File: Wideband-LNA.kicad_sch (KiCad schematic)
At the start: 23 parts, among them J1 Conn_Coaxial, J2 Conn_Coaxial, J3 USB_C_Receptacle_USB2.0_16P, U1 TQP3M9037, U2 AP2127K-ADJ

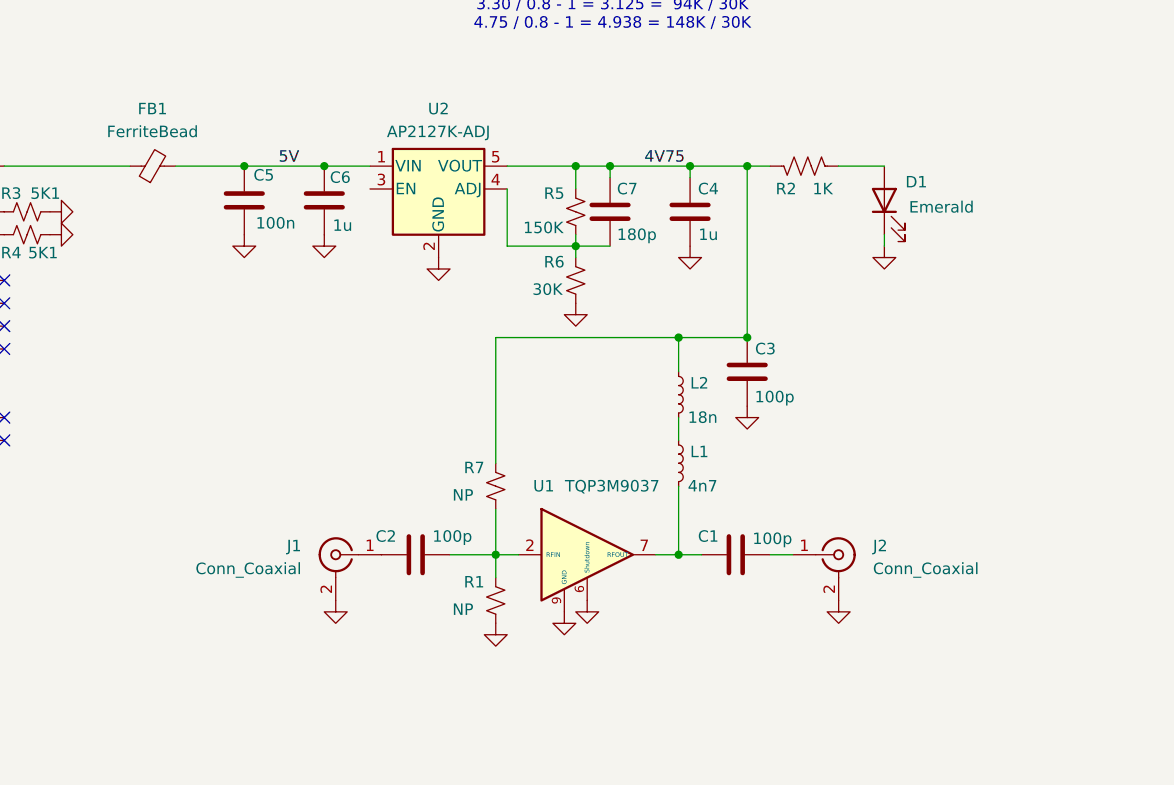
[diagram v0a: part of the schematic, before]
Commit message: rename datasheets, tweak layout
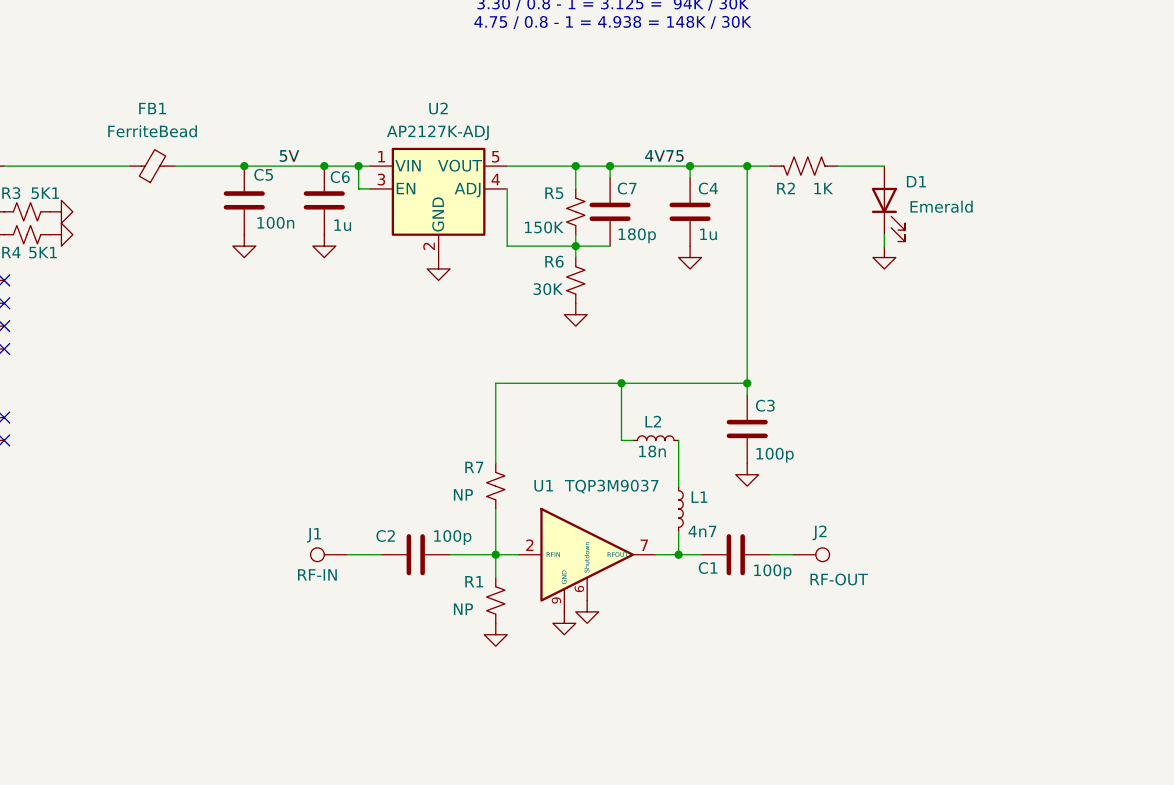
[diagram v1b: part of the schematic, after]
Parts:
- removed J1, J2: Conn_Coaxial, wa1hco:SMA_Amphenol_132289_EdgeMount, symbol Connector:Conn_Coaxial
- added J1: RF-IN, TestPoint:TestPoint_Pad_1.0x1.0mm, symbol Connector:TestPoint
- added J2: RF-OUT, TestPoint:TestPoint_Pad_1.0x1.0mm, symbol Connector:TestPoint
- J3: footprint Connector_USB:USB_C_Receptacle_HCTL_HC-TYPE-C-16P-01A -> wa1hco:USB_C_Receptacle_G-Switch_GT-USB-7010ASV
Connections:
- net 5V: now also U2.3 (EN)
- net at C1.2: now also J2.1
- net at C2.1: now also J1.1
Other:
- moved on the sheet: C3, L1, L2

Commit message: changed to 50 to 2000 MHz, qorvo 9036, 68 nH choke
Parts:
- removed R1, R7: NP, Resistor_SMD:R_0402_1005Metric, symbol Device:R_Small_US
- L2: value 18n -> 68n

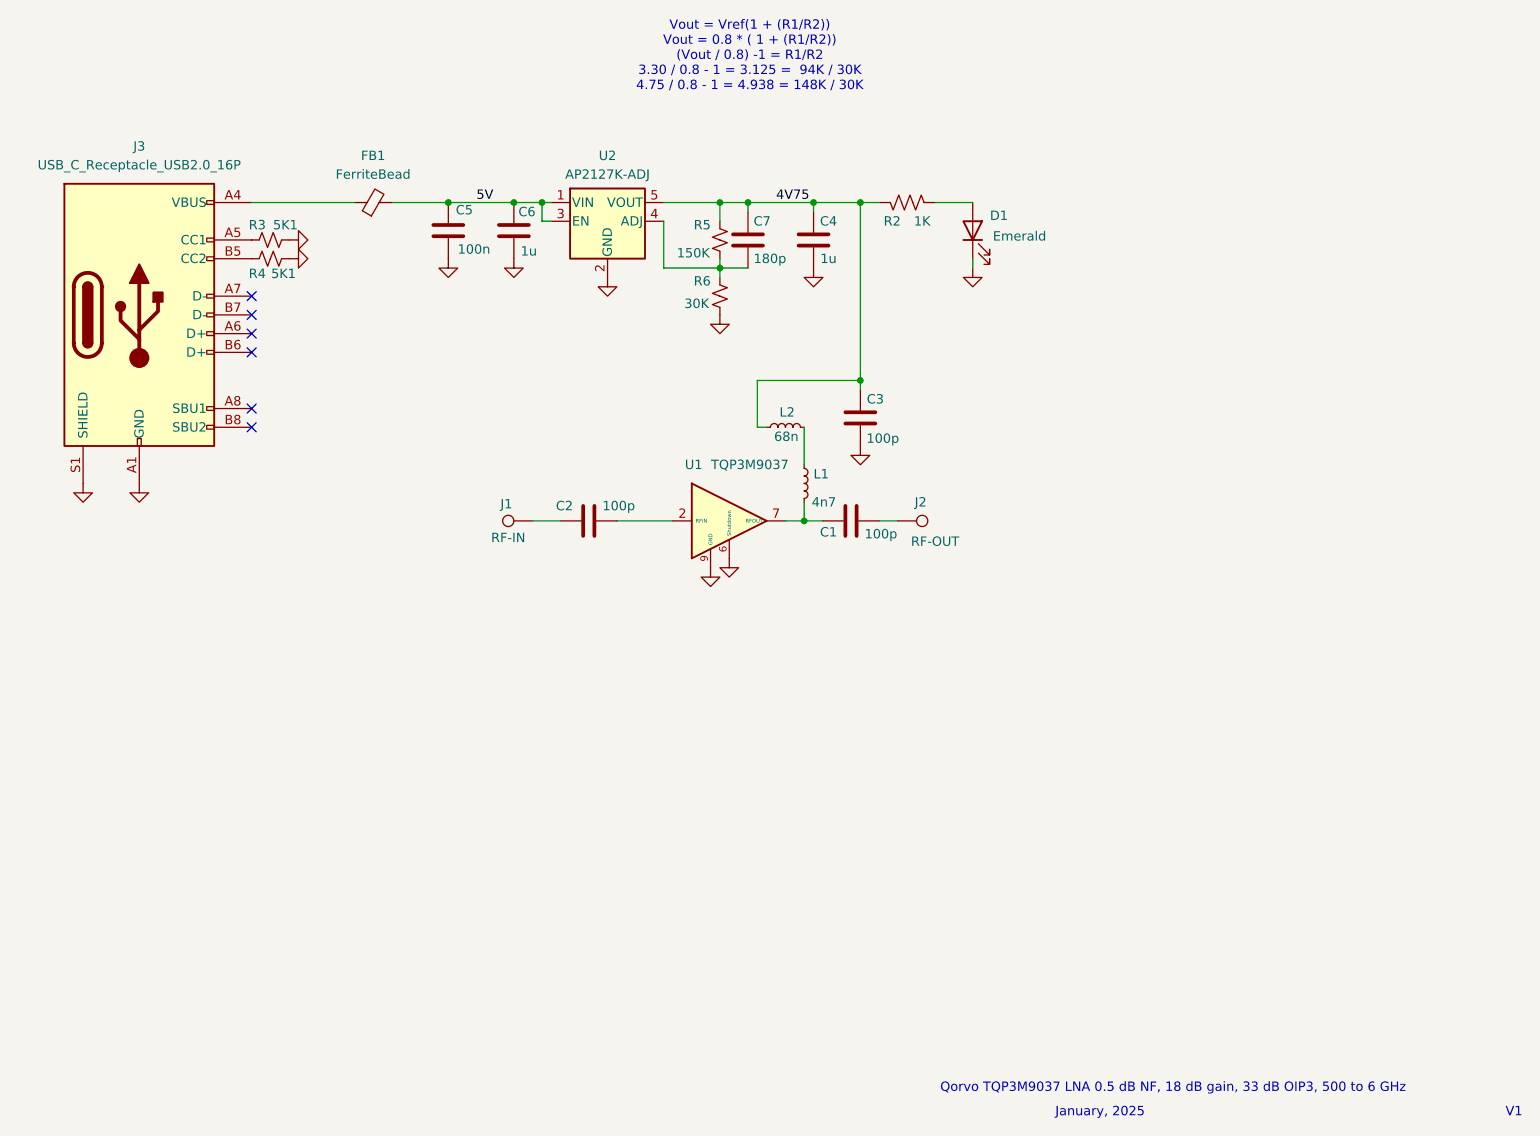
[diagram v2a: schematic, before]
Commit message: M2 screw hole from via to mounting hole Increased radius of corners Reduced side to 18.8 mm to allow clearance in enclosure Increase size of notch for SMA pin Added into to back silkscreen
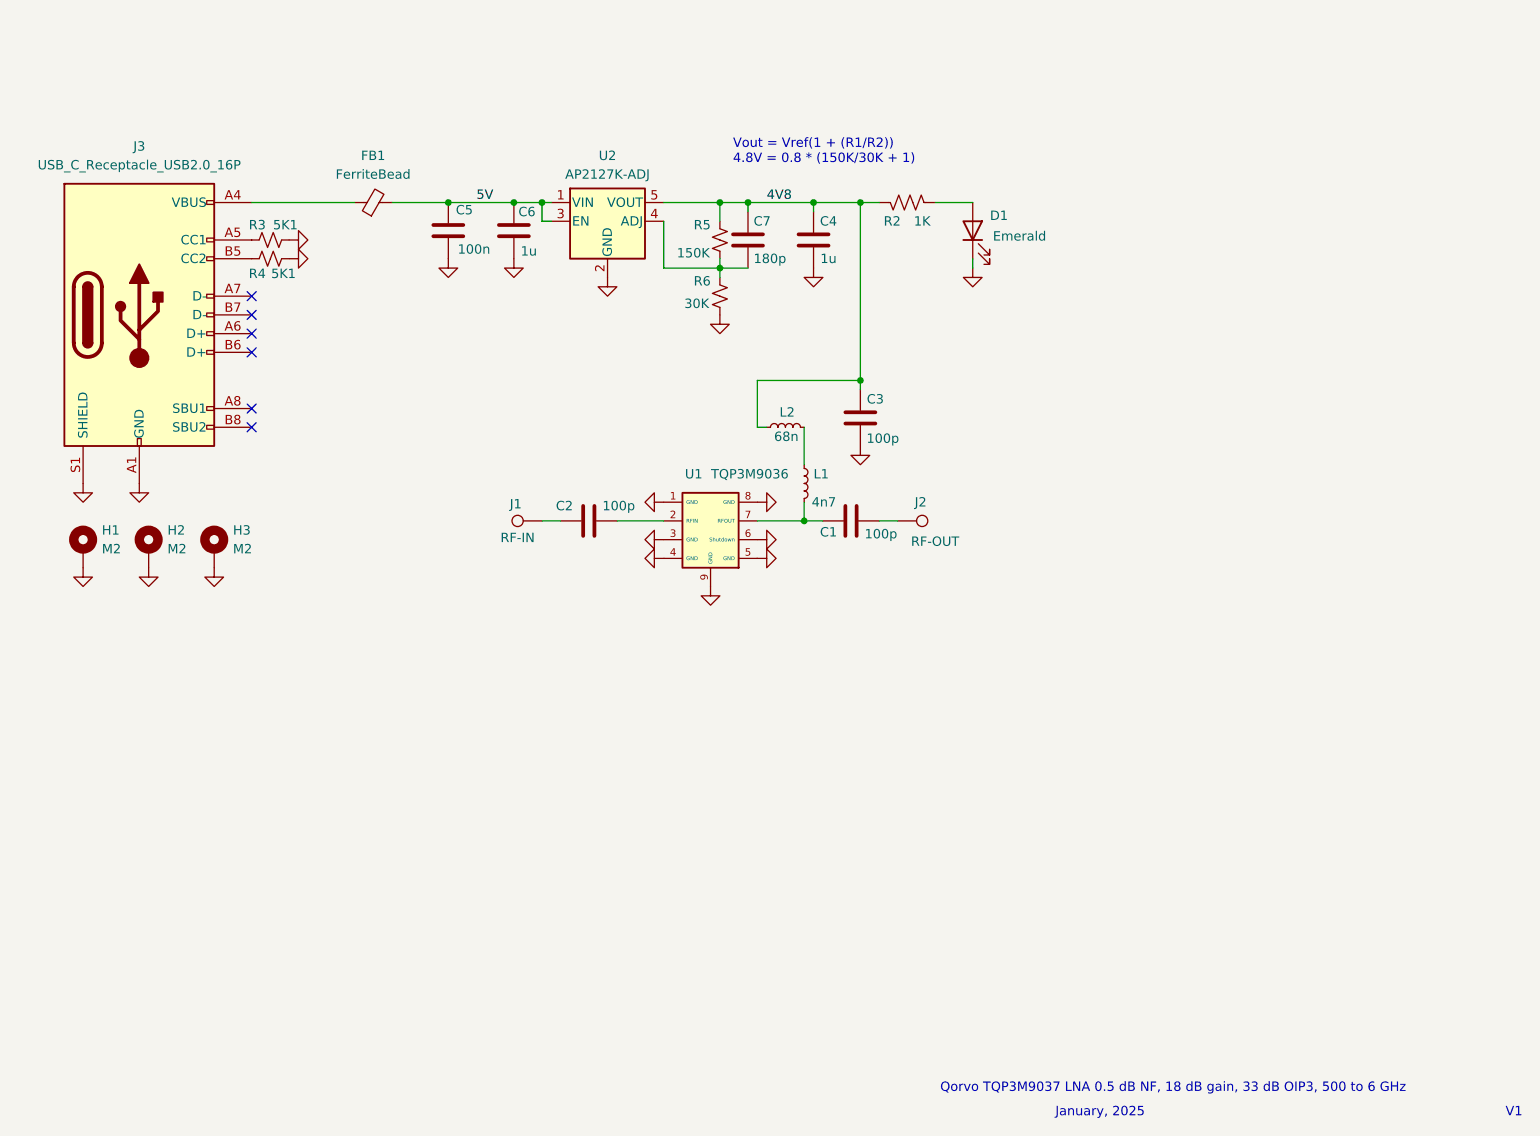
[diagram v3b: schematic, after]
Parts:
- added H1, H2, H3: M2, MountingHole:MountingHole_2.2mm_M2_DIN965_Pad, symbol Mechanical:MountingHole_Pad
- L2: LCSC C405066 -> C405073
- U1: value TQP3M9037 -> TQP3M9036; symbol wa1hco:TQP3M9037 -> wa1hco:TQP3M9036; LCSC C415712 -> C920261
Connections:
- net GND: now also U1.1 (GND), U1.3 (GND), U1.4 (GND), U1.5 (GND), U1.8 (GND), H1.1, H2.1, H3.1
- net 4V75 renamed 4V8
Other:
- note added: "Vout = Vref(1 + (R1/R2)) 4.8V = 0.8 * (150K/30K + 1)"
- note removed: "Vout = Vref(1 + (R1/R2)) Vout = 0.8 * ( 1 + (R1/R2)) (Vout / 0.8) -1 = R1/R2 3.30 / 0.8 - 1 = 3.125 = 94K / 30K 4.75 / 0.8 - 1 = 4.938 = 148K / 30K"
- moved on the sheet: J1

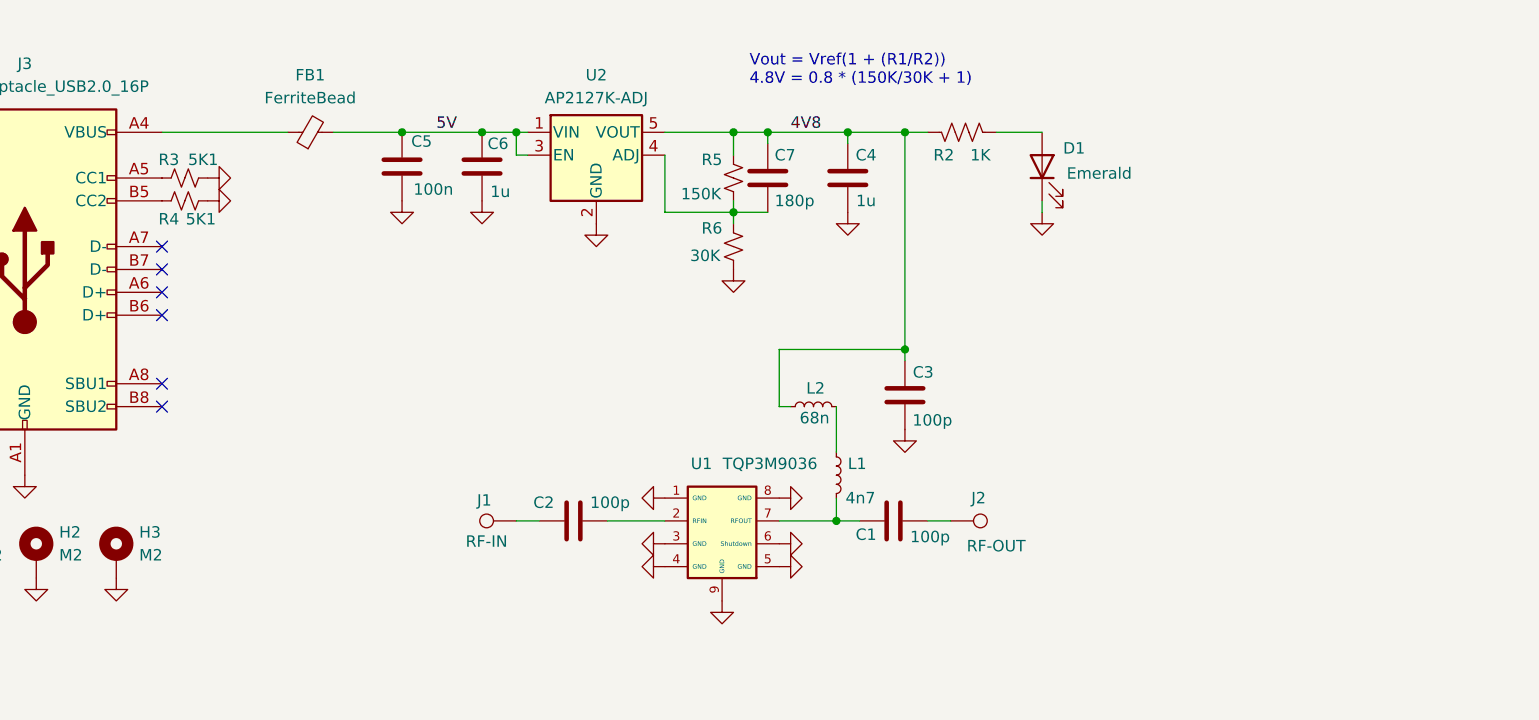
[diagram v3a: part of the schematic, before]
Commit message: added SO323 diodes to input for protection.  Added experiment for power over coax. Added id and copyright to back silkscreen. changed screw vias to mounting holes reduced size to 18.8 x 18.8 mm for tolerance.
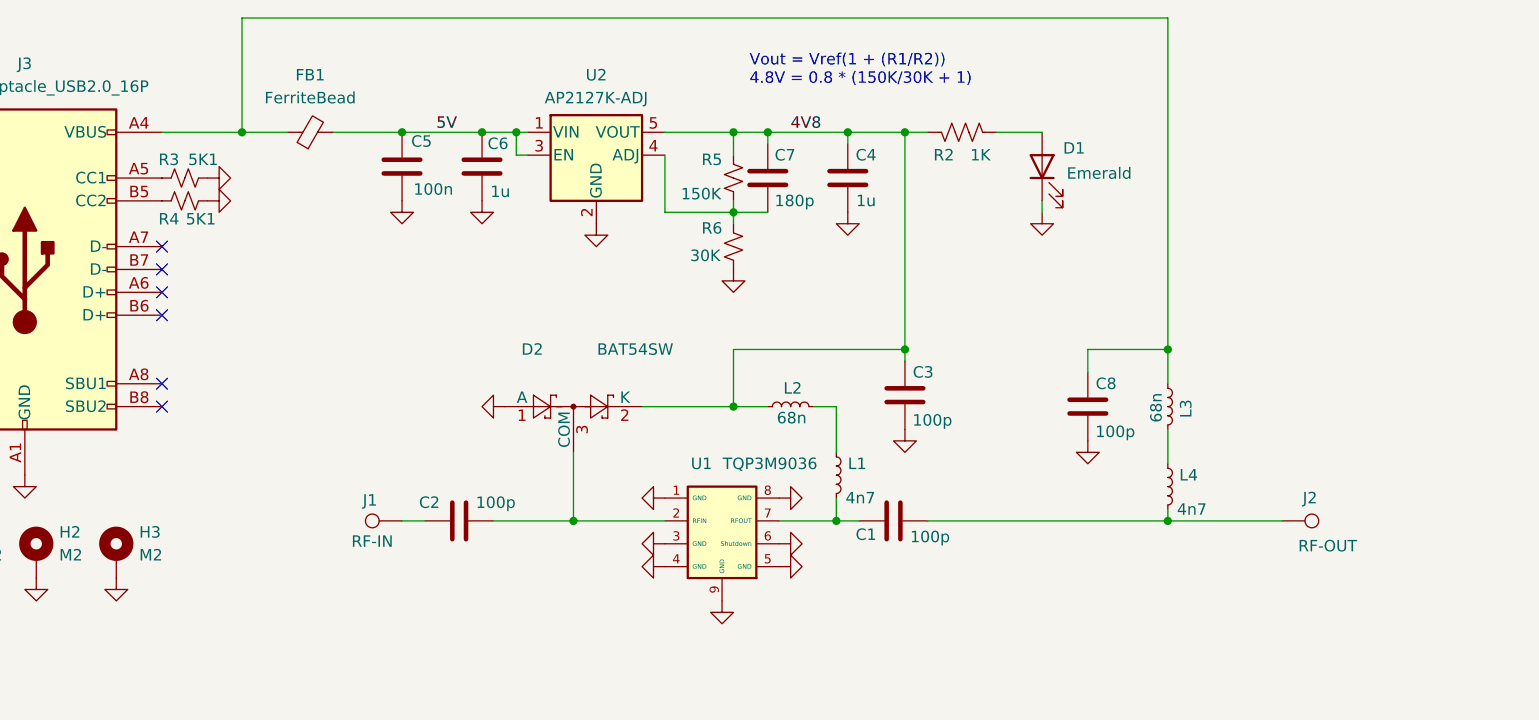
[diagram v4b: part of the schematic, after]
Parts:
- added C8: 100p, Capacitor_SMD:C_0402_1005Metric, symbol Device:C
- added D2: BAT54SW, Package_TO_SOT_SMD:SOT-323_SC-70, symbol Diode:BAT54SW
- added L3: 68n, Inductor_SMD:L_0603_1608Metric, symbol Device:L_Small
- added L4: 4n7, Inductor_SMD:L_0402_1005Metric, symbol Device:L_Small
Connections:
- net 4V8: now also D2.2 (K)
- net GND: now also C8.2, D2.1 (A)
- net at C1.2, J2.1: now also L4.2
- net at FB1.1, J3.A4 (VBUS), J3.A9 (VBUS)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: now also C8.1, L3.1
- net at C2.2, U1.2 (RFIN): now also D2.3 (COM)
- new net: L3.2, L4.1
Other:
- moved on the sheet: C2, J1, J2, L2

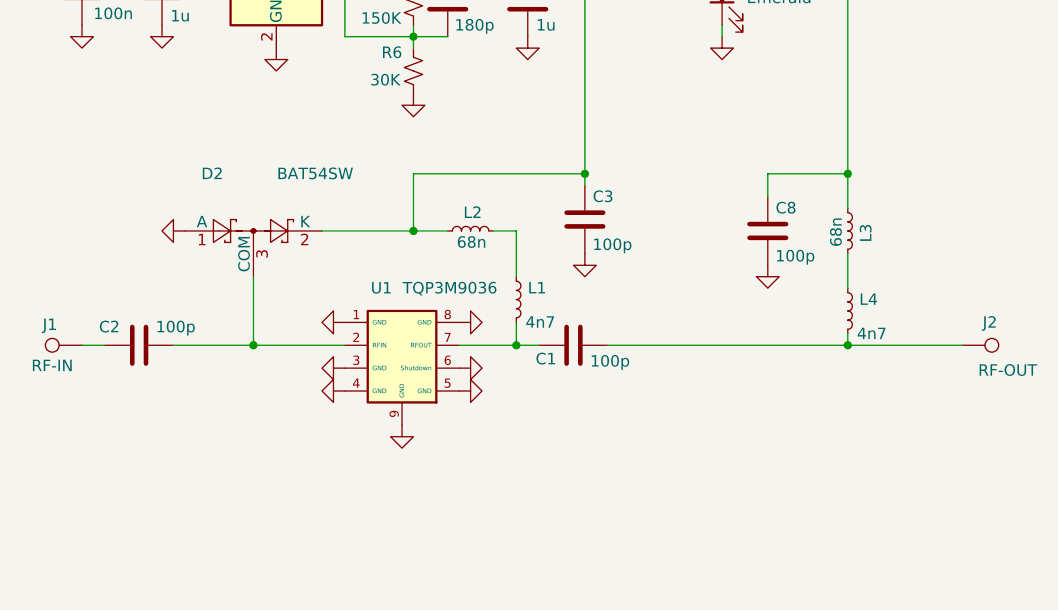
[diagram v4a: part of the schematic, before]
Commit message: Added power over output coax, forwarding to USB-C Changed input protection from OVP diodes to Inductor to ground.
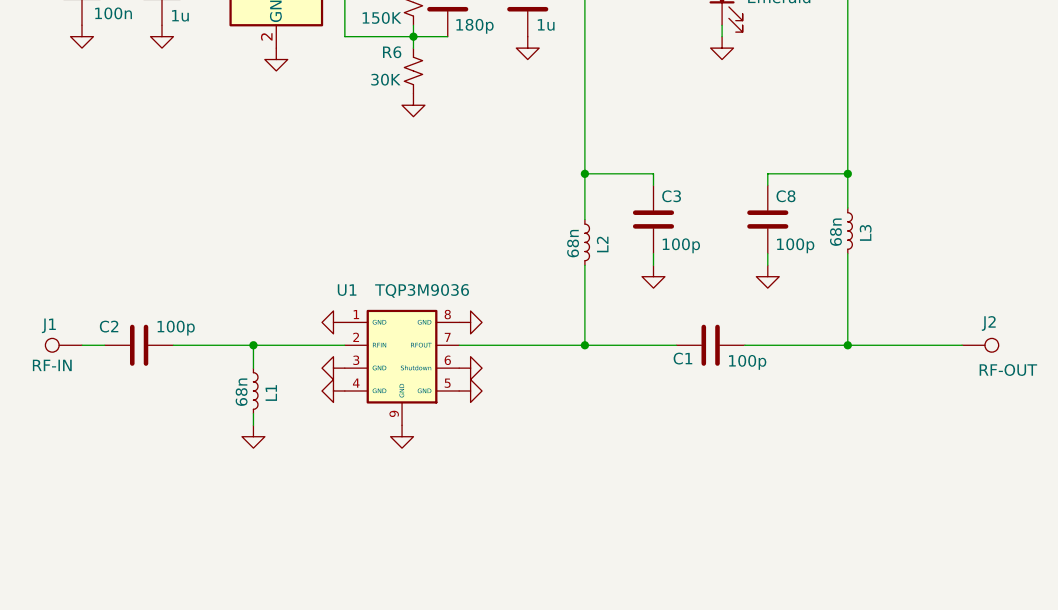
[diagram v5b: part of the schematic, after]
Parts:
- removed D2: BAT54SW, Package_TO_SOT_SMD:SOT-323_SC-70, symbol Diode:BAT54SW
- removed L4: 4n7, Inductor_SMD:L_0402_1005Metric, symbol Device:L_Small
- L1: value 4n7 -> 68n; footprint Inductor_SMD:L_0402_1005Metric -> Inductor_SMD:L_0603_1608Metric; LCSC C370225 -> C405073
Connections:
- net GND: now also L1.2
- net at L2.2: now also C1.1, U1.7 (RFOUT); no longer L1.1
- net at C1.2, J2.1: now also L3.2
- net at C2.2, U1.2 (RFIN): now also L1.1
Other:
- moved on the sheet: C1, C3, C8, L2
